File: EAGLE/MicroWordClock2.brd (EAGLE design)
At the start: 108 x 108 mm, 83 parts, among them J1 DS3231S#T&RMODULE, J2 10118193-0001LF, J3 AVR_SPI_PROG_3X2PTH, U1 ATMEGA328P

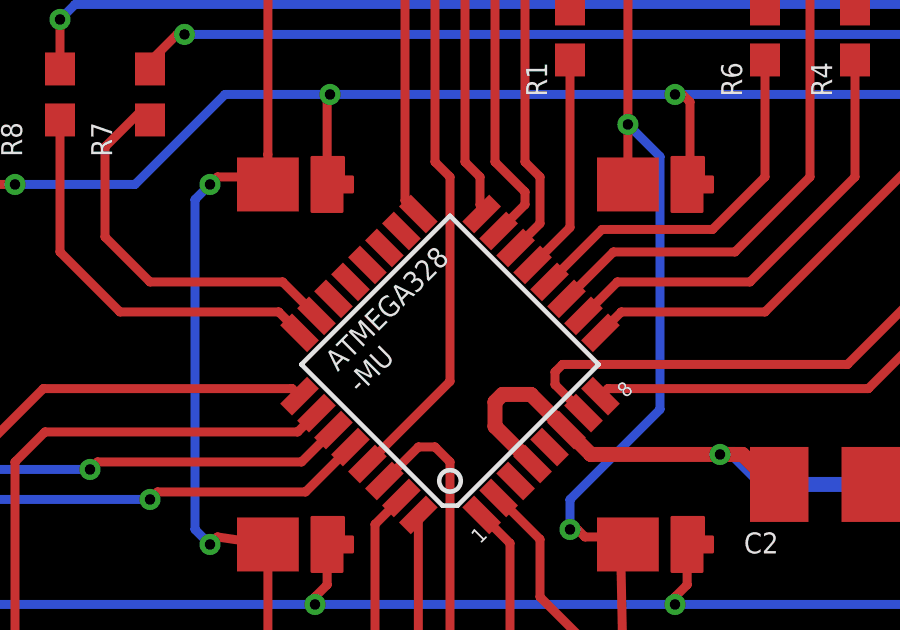
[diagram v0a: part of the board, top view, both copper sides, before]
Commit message: fixing the erc and drc of AVCC
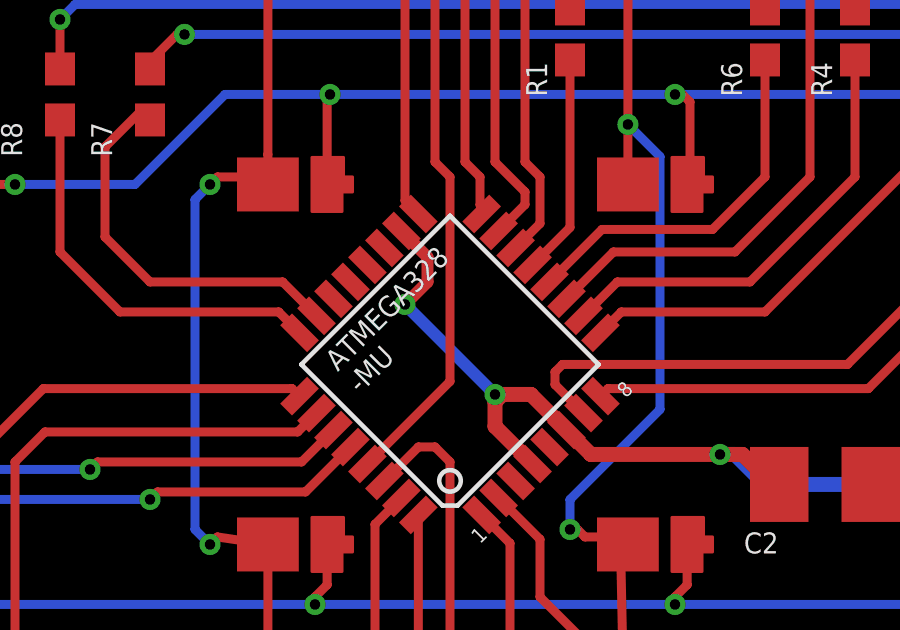
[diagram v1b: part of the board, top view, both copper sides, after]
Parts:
- U$1, U$10, U$11, U$12, U$13, U$14, U$15, U$16, U$17, U$18, U$19, U$2, U$20, U$21, U$22, U$23, U$24, U$25, U$26, U$27, U$28, U$29, U$3, U$30, U$31, U$32, U$33, U$34, U$35, U$36, U$37, U$38, U$39, U$4, U$40, U$41, U$42, U$43, U$44, U$45, U$46, U$47, U$48, U$49, U$5, U$50, U$51, U$52, U$53, U$54, U$55, U$56, U$57, U$58, U$59, U$6, U$60, U$61, U$62, U$63, U$64, U$7, U$8, U$9: value (none) -> WHITE
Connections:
- removed net AVCC: U1.18
- net +5V: now also U1.18
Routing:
- net +5V: track 335.7 -> 343.1 mm, vias 2 -> 4

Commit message: adding the dxf
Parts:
- moved C1 8.49 mm to (10.5, 63.5)
- moved C2 8.49 mm to (72.0, 56.0)
- moved C3 8.49 mm to (98.5, 12.2)
- moved C4 8.49 mm to (93.0, 14.5)
- moved J1 8.49 mm to (14.0, 62.5)
- moved J2 8.49 mm to (96.0, 7.50)
- moved J3 8.49 mm to (59.0, 112.0)
- moved L1 8.49 mm to (93.0, 12.2)
- moved R1 8.49 mm to (63.5, 71.0)
- moved R2 8.49 mm to (60.0, 48.0)
- moved R3 8.49 mm to (57.0, 48.0)
- moved R4 8.49 mm to (73.0, 71.0)
- moved R5 8.49 mm to (63.0, 48.0)
- moved R6 8.49 mm to (70.0, 71.0)
- moved R7 8.49 mm to (49.5, 69.0)
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
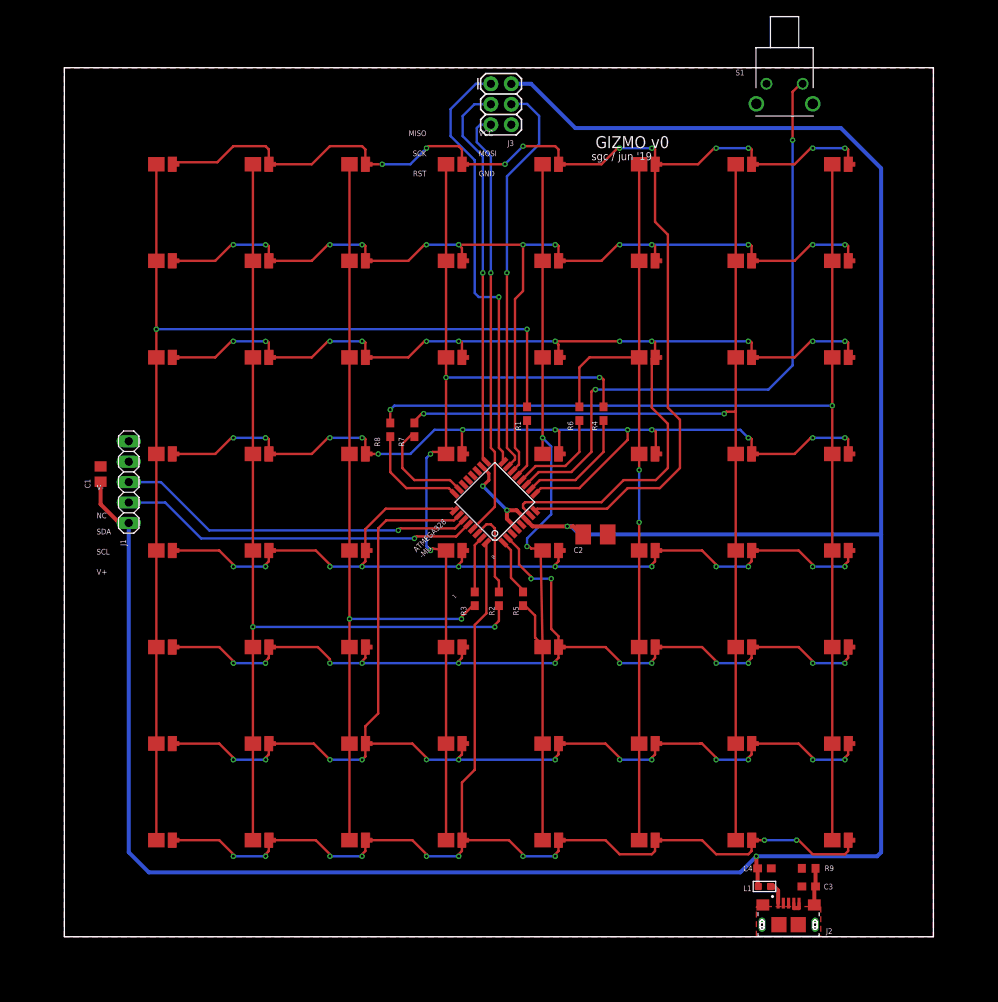
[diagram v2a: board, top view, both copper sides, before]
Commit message: half way done with rerouting
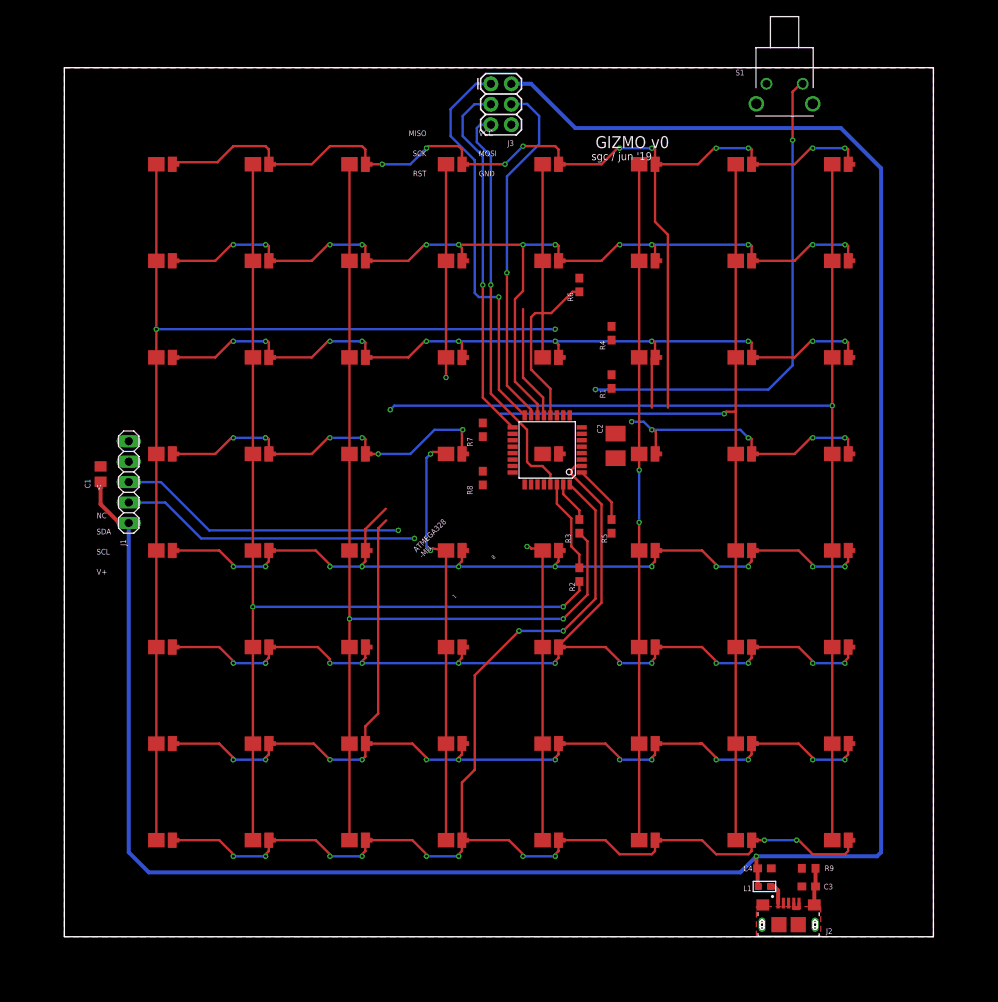
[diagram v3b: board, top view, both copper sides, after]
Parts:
- moved R6 16.0 mm to (70.0, 87.0)
- moved R3 15.8 mm to (70.0, 57.0)
- moved R5 14.2 mm to (74.0, 57.0)
- moved R8 13.0 mm to (58.0, 63.0)
- moved C2 11.3 mm to (74.5, 67.0), turned to 90 degrees
- moved R1 11.2 mm to (74.0, 75.0)
- moved R2 10.4 mm to (70.0, 51.0)
- moved R4 10.0 mm to (74.0, 81.0)
- moved U1 9.19 mm to (66.0, 66.5), turned to 180 degrees
- moved R7 8.50 mm to (58.0, 69.0)
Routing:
- net +5V: track 343.1 -> 282.9 mm, vias 4 -> 1
- net ROW4: track 121.4 -> 82.3 mm, vias 12 -> 11
- net N$7: track 95.9 -> 62.4 mm, vias 2 -> 1
- net N$6: track 111.6 -> 79.2 mm, vias 4 -> 3
- net ROW3: track 138.4 -> 108.4 mm, vias 12 -> 11
- net ROW1: track 163.2 -> 134.9 mm
- net N$5: track 100.4 -> 123.1 mm
- net N$1: track 79.3 -> 61.4 mm
- net ROW8: track 139.9 -> 157.3 mm, vias 10 -> 12
- net COL4: track 14.9 -> 0.00 mm
- net COL8: track 13.7 -> 0.00 mm
- net COL7: track 13.2 -> 0.00 mm
- net N$8: track 96.8 -> 84.0 mm
- net N$9: track 124.7 -> 113.4 mm, vias 2 -> 1
- net ROW6: track 119.8 -> 129.4 mm, vias 14 -> 12
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
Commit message: done rerouting everything except for power
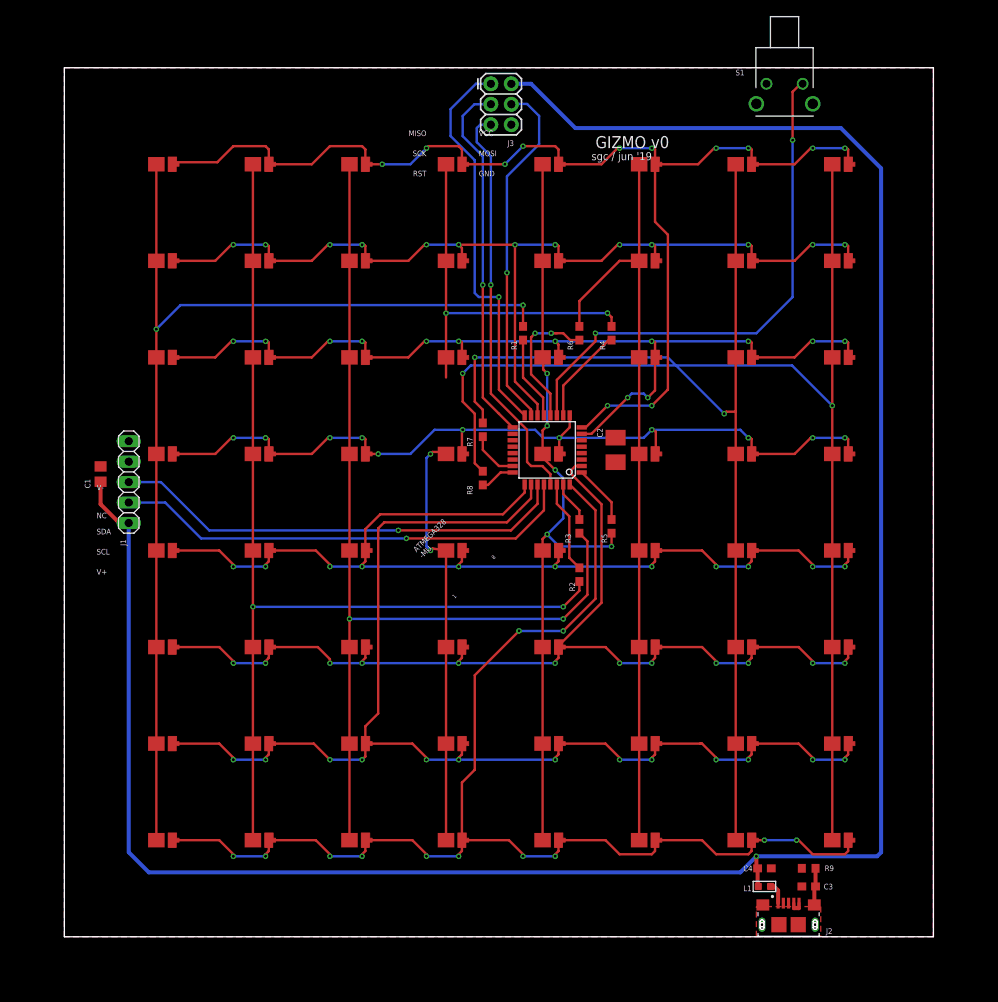
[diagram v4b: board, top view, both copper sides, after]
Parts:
- moved R1 12.5 mm to (63.0, 81.0)
- moved R6 6.00 mm to (70.0, 81.0)
- moved C2 0.50 mm to (74.5, 66.5)
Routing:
- net N$7: track 62.4 -> 97.0 mm, vias 1 -> 5
- net ROW4: track 82.3 -> 108.7 mm
- net N$6: track 79.2 -> 101.2 mm, vias 3 -> 4
- net SDA: track 36.0 -> 57.1 mm
- net ROW7: track 131.3 -> 152.1 mm
- net SCL: track 37.3 -> 58.1 mm
- net ROW5: track 107.7 -> 126.8 mm
- net N$9: track 113.4 -> 128.0 mm, vias 1 -> 2
- net N$8: track 84.0 -> 96.7 mm, vias 2 -> 0
- net COL4: track 0.00 -> 12.0 mm
- net ROW1: track 134.9 -> 145.3 mm, vias 10 -> 12
- net ROW3: track 108.4 -> 118.2 mm, vias 11 -> 13
- net EE: track 139.1 -> 145.6 mm
- net COL7: track 0.00 -> 6.19 mm
- net COL8: track 0.00 -> 4.35 mm
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
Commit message: initial routing + pours. created a variant for the no pops
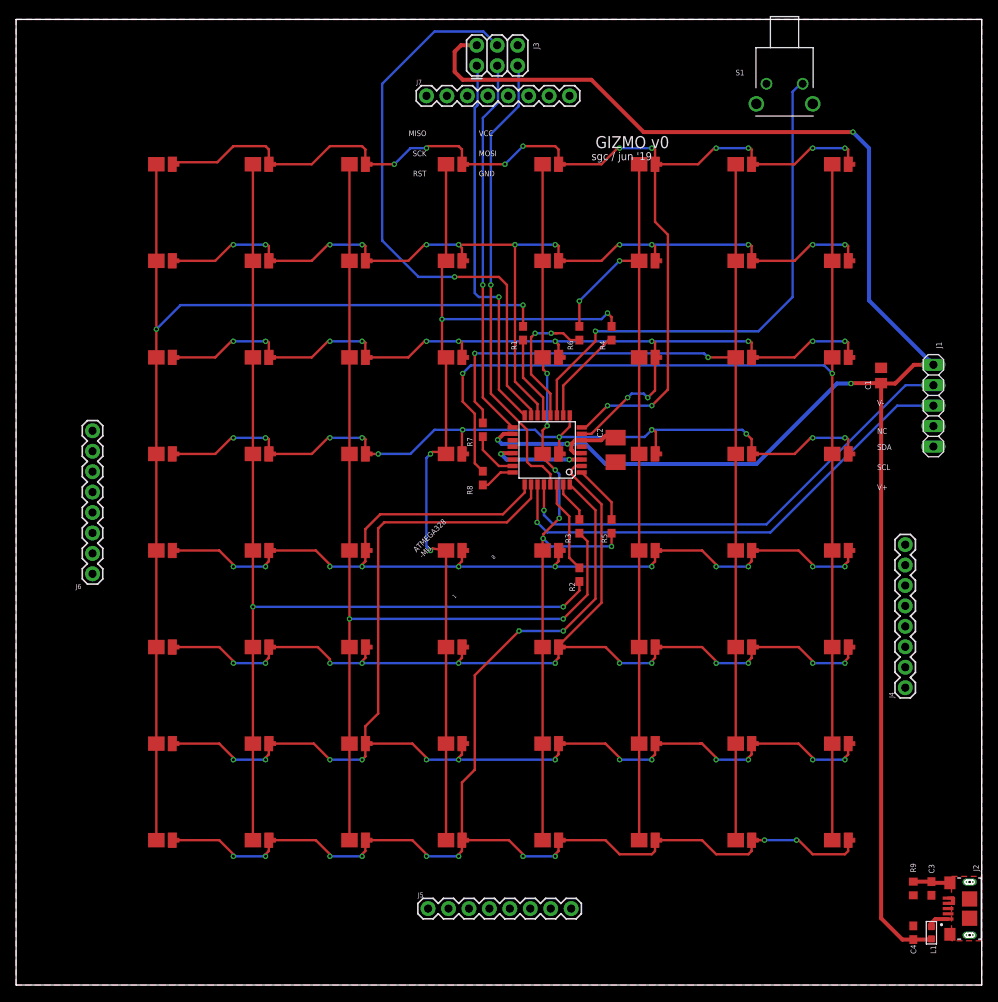
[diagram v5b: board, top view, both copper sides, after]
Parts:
- added J4, J5, J6, J7: (no value), SparkFun-Connectors:1X08
- moved J1 100.5 mm to (114.0, 72.0), turned to 270 degrees
- moved C1 97.8 mm to (107.5, 75.8)
- moved J2 22.6 mm to (118.5, 9.50), turned to 90 degrees
- moved L1 21.5 mm to (113.8, 6.50), turned to 270 degrees
- moved C4 20.2 mm to (111.5, 6.50), turned to 90 degrees
- moved C3 15.3 mm to (113.8, 12.0), turned to 90 degrees
- moved R9 13.2 mm to (111.5, 12.0), turned to 270 degrees
- moved J3 2.85 mm to (57.2, 114.2), turned to 0 degrees
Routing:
- net +5V: track 282.9 -> 236.5 mm, vias 1 -> 4
- net MOSI: track 44.2 -> 72.4 mm
- net GND: track 2.25 -> 13.8 mm, vias 0 -> 2
- net N$6: track 101.2 -> 111.7 mm
- net RESET: track 50.8 -> 57.4 mm
- net SDA: track 57.1 -> 61.0 mm
- net N$9: track 128.0 -> 125.7 mm
- net MISO: track 49.6 -> 47.7 mm
- net SCK: track 45.4 -> 47.3 mm
- net SCL: track 58.1 -> 59.8 mm
- net EE: track 145.6 -> 143.9 mm
- net ROW3: track 118.2 -> 117.6 mm
- net N$7: track 97.0 -> 96.8 mm, vias 5 -> 6
- net N$1: track 65.7 -> 65.9 mm, vias 2 -> 1
- net N$8: vias 0 -> 2
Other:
- board size 108 x 108 mm -> 120 x 120 mm

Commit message: fixing up the lettering
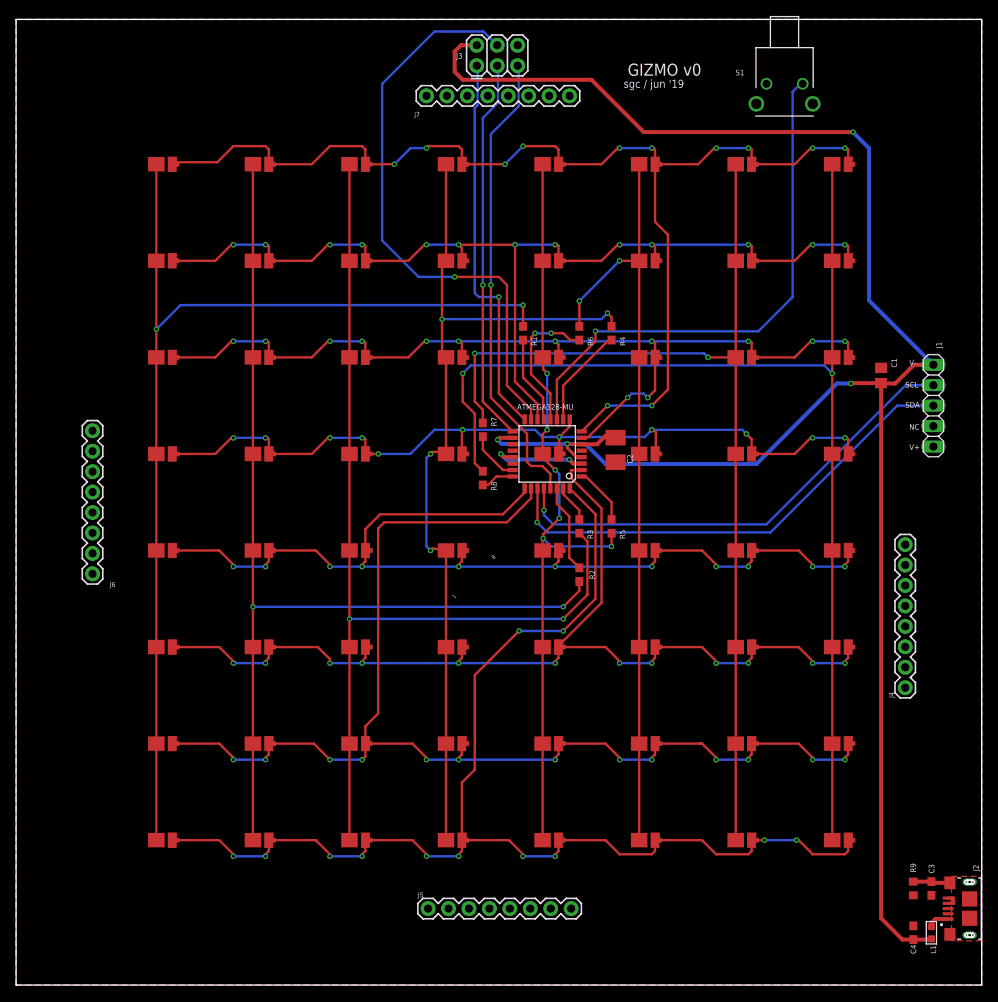
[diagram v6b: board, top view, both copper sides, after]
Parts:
- moved U1 0.50 mm to (66.0, 66.0)
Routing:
- net SDA: track 61.0 -> 60.5 mm
- net SCL: track 59.8 -> 59.3 mm
- net SCK: track 47.3 -> 47.8 mm
- net ROW8: track 157.3 -> 156.8 mm
- net ROW7: track 152.1 -> 151.6 mm
- net ROW5: track 126.8 -> 126.3 mm
- net ROW4: track 108.6 -> 108.1 mm
- net ROW2: track 124.6 -> 125.1 mm
- net RESET: track 57.4 -> 57.9 mm
- net N$1: track 65.9 -> 66.4 mm
- net MOSI: track 72.4 -> 72.9 mm
- net MISO: track 47.7 -> 48.2 mm
- net COL6: track 17.3 -> 17.8 mm
- net COL4: track 12.0 -> 12.5 mm
- net COL3: track 5.19 -> 4.69 mm
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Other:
- board text added: "5V MICRO USB"
- board text added: "ATMEGA328-MU"
- board text removed: "ATMEGA328 -MU"

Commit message: Fixing initial bugs from V0 - pad sizes, SCL/SDA line switch see issue #4 for full list. Also added updated schematic"
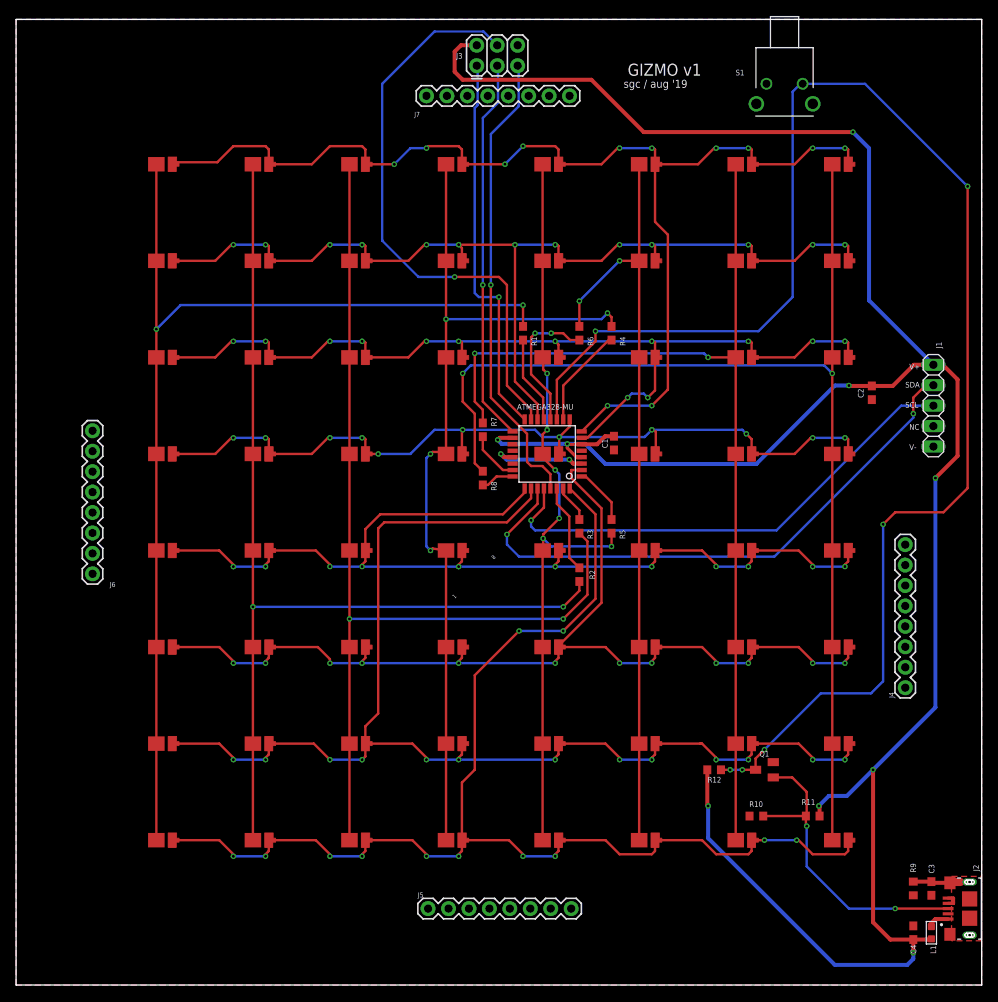
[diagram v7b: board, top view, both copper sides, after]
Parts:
- added Q1: 2N7002, 2N7002:SOT23
- added R10, R11, R12: TBD, rcl:R0603
- C1: device rcl:C0805 -> rcl:C0603
- C2: device rcl:B/3528-21R -> rcl:C0603
- R1, R2, R3, R4, R5, R6, R7, R8: value 470 -> 51
- moved C1 34.2 mm to (74.3, 67.3), turned to 270 degrees
- moved C2 32.6 mm to (106.3, 73.6), turned to 270 degrees
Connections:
- new net SWITCH: Q1.3, R12.1, S1.1, U1.11
- net +5V: now also C2.1, R11.2, R12.2; no longer C2.+
- net GND: now also C2.2, Q1.2, R10.1; no longer C2.-
- net N$1: now also J2.3, Q1.1, R10.2, R11.1; no longer S1.1, U1.11
- net SCL: now also J1.3; no longer J1.2
- net SDA: now also J1.2; no longer J1.3
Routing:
- net SWITCH: track 0.00 -> 187.0 mm, vias 0 -> 6
- net +5V: track 237.0 -> 299.7 mm, vias 4 -> 9
- net N$1: track 66.4 -> 39.3 mm, vias 1 -> 2
- net SDA: track 60.5 -> 72.4 mm, vias 1 -> 2
- net SCL: track 59.3 -> 62.0 mm
- net PE: track 4.83 -> 6.19 mm
- net N$6: track 111.7 -> 110.7 mm
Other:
- board text added: "GIZMO v1"
- board text added: "sgc / aug '19"
- board text removed: "GIZMO v0"
- board text removed: "sgc / jun '19"
